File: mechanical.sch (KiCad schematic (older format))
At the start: 44 parts

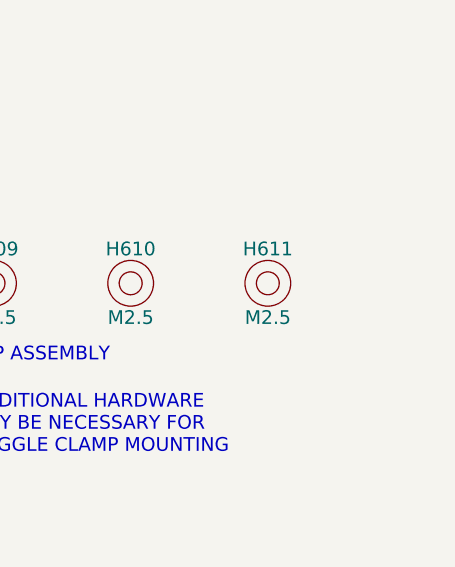
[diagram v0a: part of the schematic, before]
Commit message: passes drc except for qfn footprint...
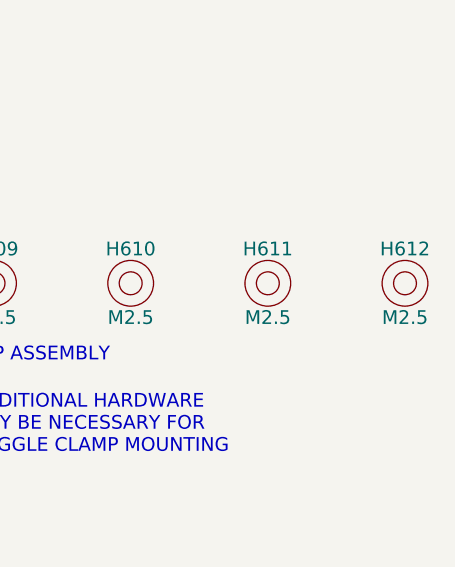
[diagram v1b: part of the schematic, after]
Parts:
- added H612: M2.5, tm-kicad-lib:MountingHole_2-5mm, symbol HOLE
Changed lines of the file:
@@
 	1    0    0    1
 $EndComp
+$Comp
+L HOLE H612
+U 1 1 554BDF1B
+P 8500 3650
+F 0 "H612" H 8500 3800 60  0000 C CNN
+F 1 "M2.5" H 8500 3500 60  0000 C CNN
+F 2 "tm-kicad-lib:MountingHole_2-5mm" H 8500 3650 60  0001 C CNN
+F 3 "" H 8500 3650 60  0000 C CNN
+	1    8500 3650
+	1    0    0    -1
+$EndComp
 $EndSCHEMATC

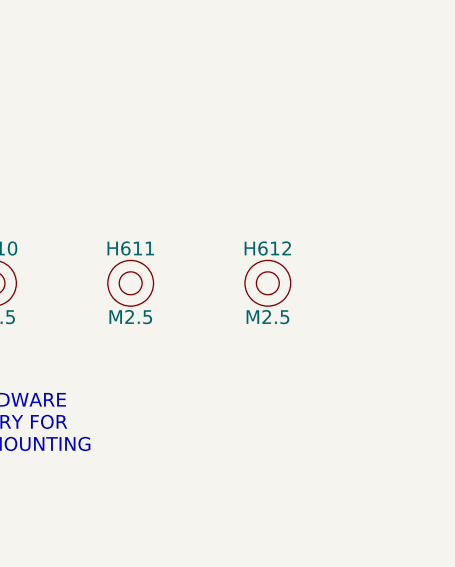
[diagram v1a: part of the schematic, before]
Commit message: qfn swapped, another mount hole added, passes drc
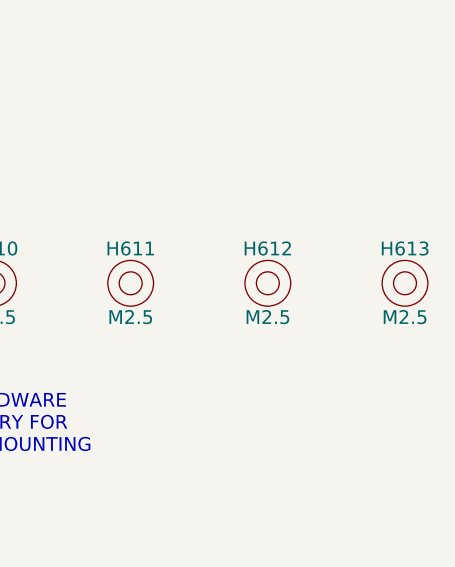
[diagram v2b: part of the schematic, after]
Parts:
- added H613: M2.5, tm-kicad-lib:MountingHole_2-5mm, symbol HOLE
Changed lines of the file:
@@
+	1    0    0    -1
+$EndComp
+$Comp
+L HOLE H613
+U 1 1 554BFB2E
+P 9100 3650
+F 0 "H613" H 9100 3800 60  0000 C CNN
+F 1 "M2.5" H 9100 3500 60  0000 C CNN
+F 2 "tm-kicad-lib:MountingHole_2-5mm" H 9100 3650 60  0001 C CNN
+F 3 "" H 9100 3650 60  0000 C CNN
+	1    9100 3650
 	1    0    0    -1
 $EndComp

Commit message: still easier access to usb
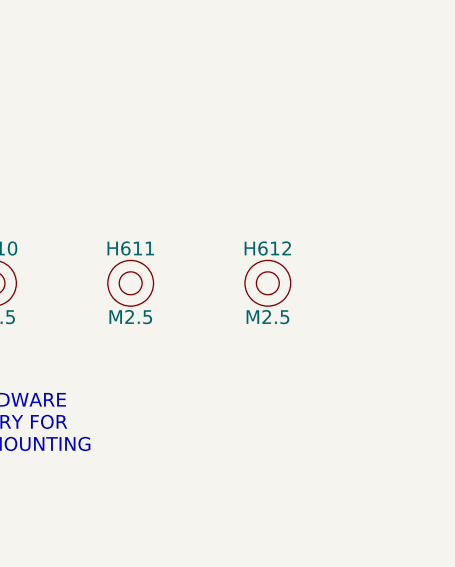
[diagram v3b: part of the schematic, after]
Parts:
- removed H613: M2.5, tm-kicad-lib:MountingHole_2-5mm, symbol HOLE
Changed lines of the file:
@@
-	1    0    0    -1
-$EndComp
-$Comp
-L HOLE H613
-U 1 1 554BFB2E
-P 9100 3650
-F 0 "H613" H 9100 3800 60  0000 C CNN
-F 1 "M2.5" H 9100 3500 60  0000 C CNN
-F 2 "tm-kicad-lib:MountingHole_2-5mm" H 9100 3650 60  0001 C CNN
-F 3 "" H 9100 3650 60  0000 C CNN
-	1    9100 3650
 	1    0    0    -1
 $EndComp
